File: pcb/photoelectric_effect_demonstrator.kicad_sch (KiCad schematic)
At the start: 0 parts

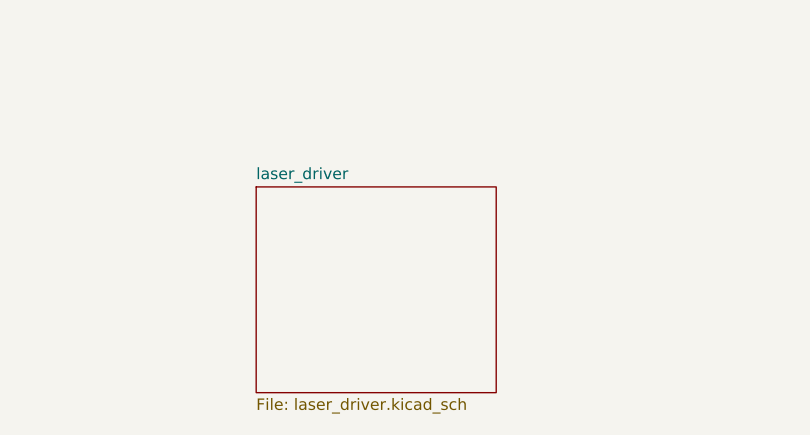
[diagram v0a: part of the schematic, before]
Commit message: refactor: removed the laser component of the project
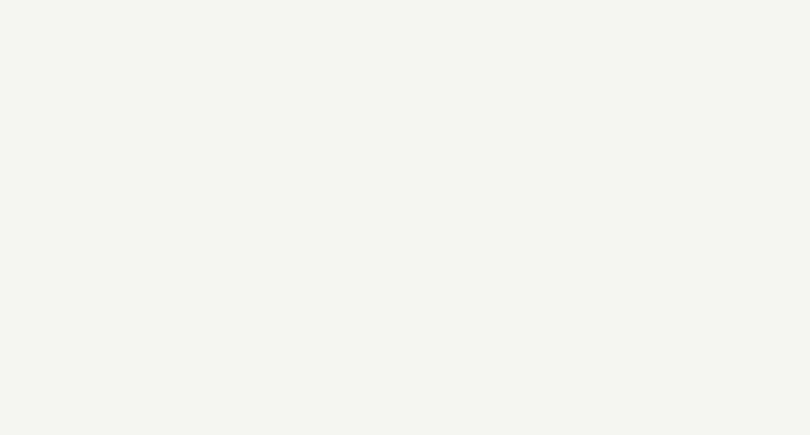
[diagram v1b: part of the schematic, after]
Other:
- removed sheet laser_driver
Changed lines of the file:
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@@
 		)
 		(instances
-			(project "photoelectric_demonstrator"
+			(project "photoelectric_effect_demonstrator"
 				(path "/02a3d1a0-aaa6-4aef-8c62-d71953fb14c6"
 					(page "7")
-				)
-			)
-		)
-	)
-	(sheet
-		(at 137.16 187.96)
-		(size 26.67 22.86)
-		(exclude_from_sim no)
-		(in_bom yes)
-		(on_board yes)
-		(dnp no)
-		(fields_autoplaced yes)
-		(stroke
-			(width 0.1524)
-			(type solid)
-		)
-		(fill
-			(color 0 0 0 0.0000)
-		)
-		(property "Sheetname" "laser_driver"
-			(at 137.16 187.2484 0)
-			(effects
-				(font
-					(size 1.27 1.27)
-				)
-				(justify left bottom)
-			)
-		)
-		(property "Sheetfile" "laser_driver.kicad_sch"
-			(at 137.16 211.4046 0)
-			(effects
-				(font
-					(size 1.27 1.27)
-				)
-				(justify left top)
-			)
-		)
-		(instances
-			(project "photoelectric_demonstrator"
-				(path "/02a3d1a0-aaa6-4aef-8c62-d71953fb14c6"
-					(page "17")
 				)
 			)
@@
 		)
 		(instances
-			(project "photoelectric_demonstrator"
+			(project "photoelectric_effect_demonstrator"
 				(path "/02a3d1a0-aaa6-4aef-8c62-d71953fb14c6"
 					(page "8")
@@
 		)
 		(instances
-			(project "photoelectric_demonstrator"
+			(project "photoelectric_effect_demonstrator"
 				(path "/02a3d1a0-aaa6-4aef-8c62-d71953fb14c6"
 					(page "6")
@@
 		)
 		(instances
-			(project "photoelectric_demonstrator"
+			(project "photoelectric_effect_demonstrator"
 				(path "/02a3d1a0-aaa6-4aef-8c62-d71953fb14c6"
 					(page "3")
@@
 		)
 		(instances
-			(project "photoelectric_demonstrator"
+			(project "photoelectric_effect_demonstrator"
 				(path "/02a3d1a0-aaa6-4aef-8c62-d71953fb14c6"
 					(page "4")
@@
 		)
 		(instances
-			(project "photoelectric_demonstrator"
+			(project "photoelectric_effect_demonstrator"
 				(path "/02a3d1a0-aaa6-4aef-8c62-d71953fb14c6"
 					(page "16")
@@
 		)
 		(instances
-			(project "photoelectric_demonstrator"
+			(project "photoelectric_effect_demonstrator"
 				(path "/02a3d1a0-aaa6-4aef-8c62-d71953fb14c6"
 					(page "8")
@@
 		)
 		(instances
-			(project "photoelectric_demonstrator"
+			(project "photoelectric_effect_demonstrator"
 				(path "/02a3d1a0-aaa6-4aef-8c62-d71953fb14c6"
 					(page "2")
